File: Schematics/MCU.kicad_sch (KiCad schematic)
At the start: 24 parts, among them U1 STM32F405RGTx

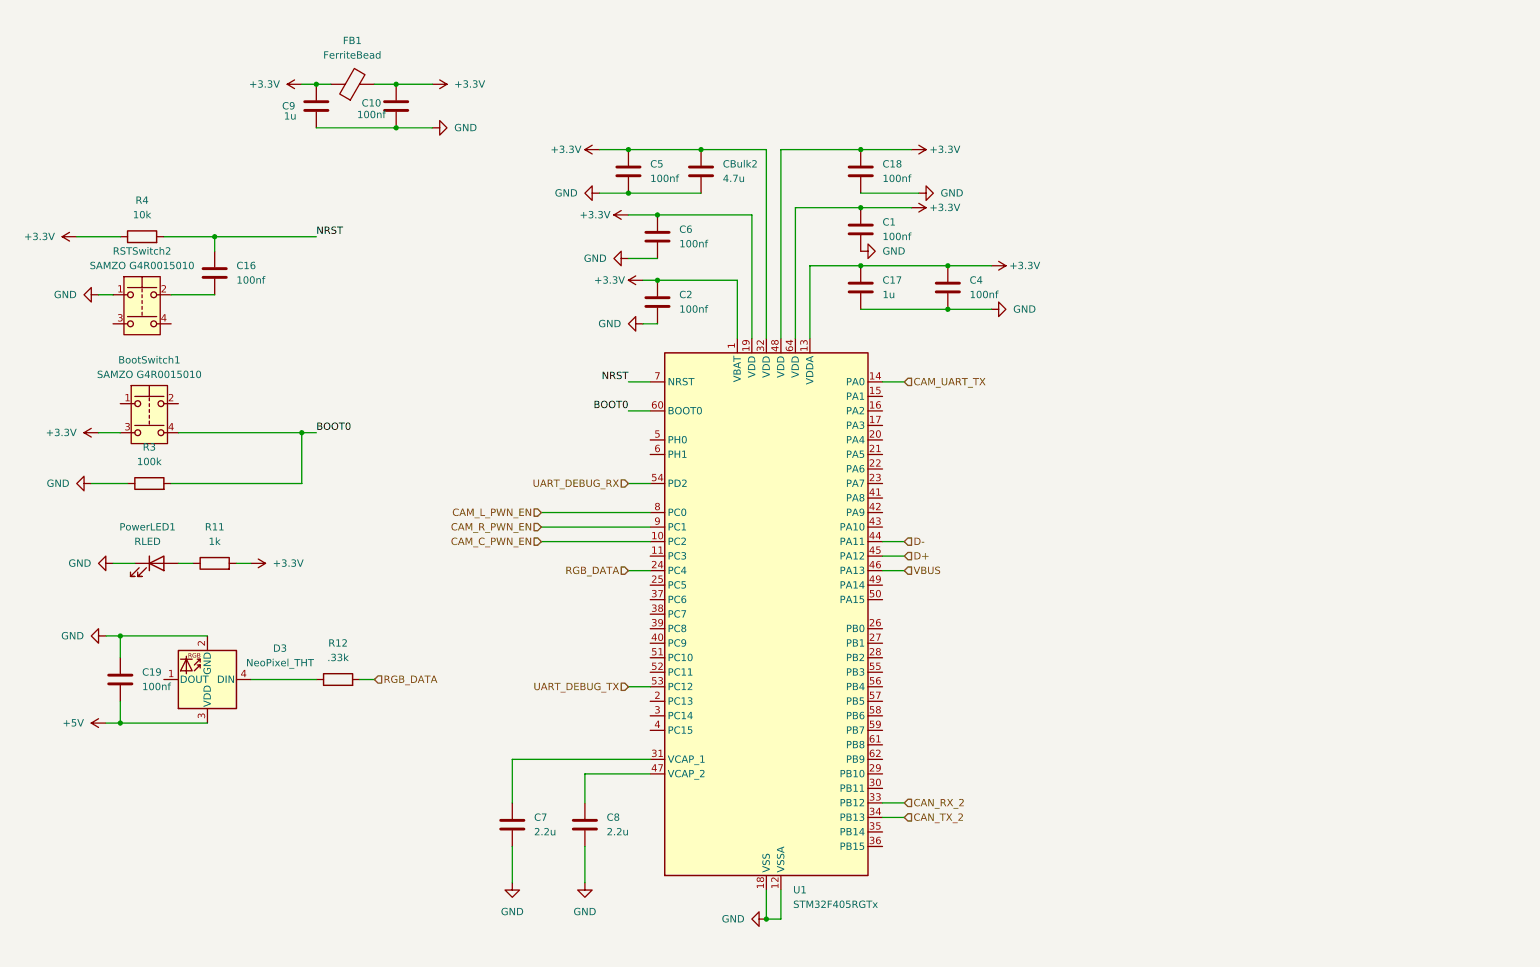
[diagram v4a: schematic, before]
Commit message: routing taking place only USB to do
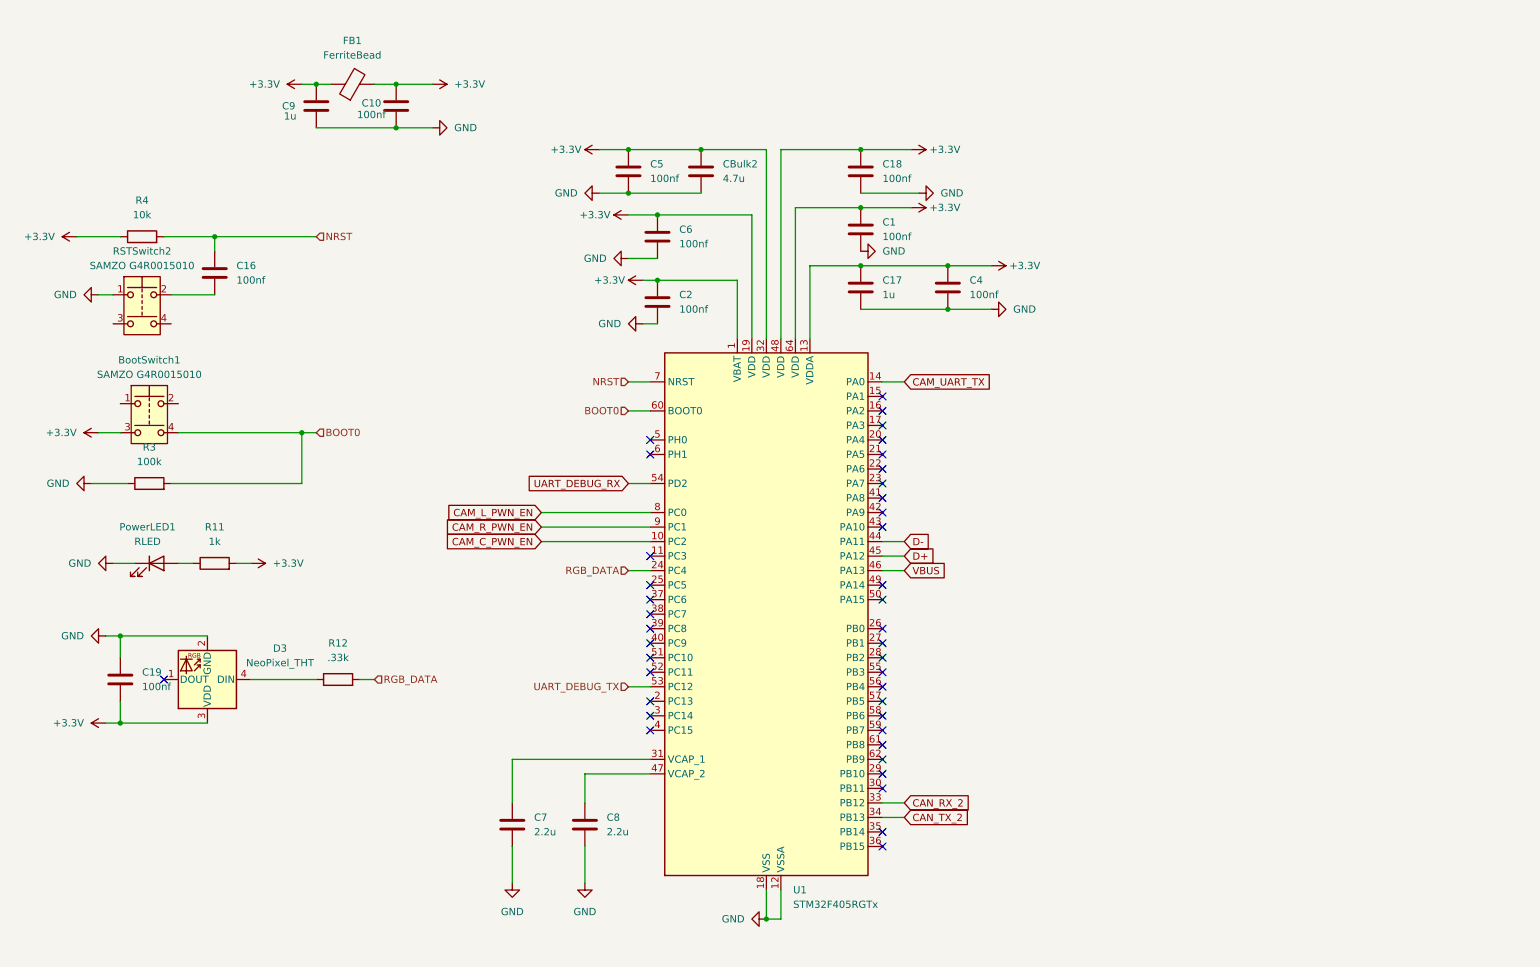
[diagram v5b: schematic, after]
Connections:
- net +5V is gone; now on net +3.3V: C19.2, D3.3 (VDD)
- no-connect marks 0 -> 40

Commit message: Cleaned up schematic added ocilator added jtag 10 pin begining routing again
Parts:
- added C21, C22: 18p, Capacitor_SMD:C_0603_1608Metric_Pad1.08x0.95mm_HandSolder, symbol Device:C
- added J1: Microsemi_FlashPro-JTAG-10, myFootprints:CONN_7024610XX_MOL, symbol Connector:Microsemi_FlashPro-JTAG-10
- added Y1: 8mhz, Crystal:Crystal_SMD_3225-4Pin_3.2x2.5mm_HandSoldering, symbol Device:Crystal_GND24
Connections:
- net +3.3V: no longer C10.2, C17.1, C4.1, FB1.2, U1.13 (VDDA)
- net GND: now also C21.2, C22.2, Y1.2, Y1.4
- net OSC IN: now reaches U1.5 (PH0)
- net OSC IN: now also C21.1, Y1.1
- net OSC OUT: now reaches U1.6 (PH1)
- net OSC OUT: now also C22.1, Y1.3
- new net: J1.10 (GND), J1.2 (GND)
- new net +3.3VA: C10.2, C17.1, C4.1, FB1.2, U1.13 (VDDA)
- no-connect marks 40 -> 38
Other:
- moved on the sheet: BootSwitch1, C19, D3, PowerLED1, R11, R12, R3

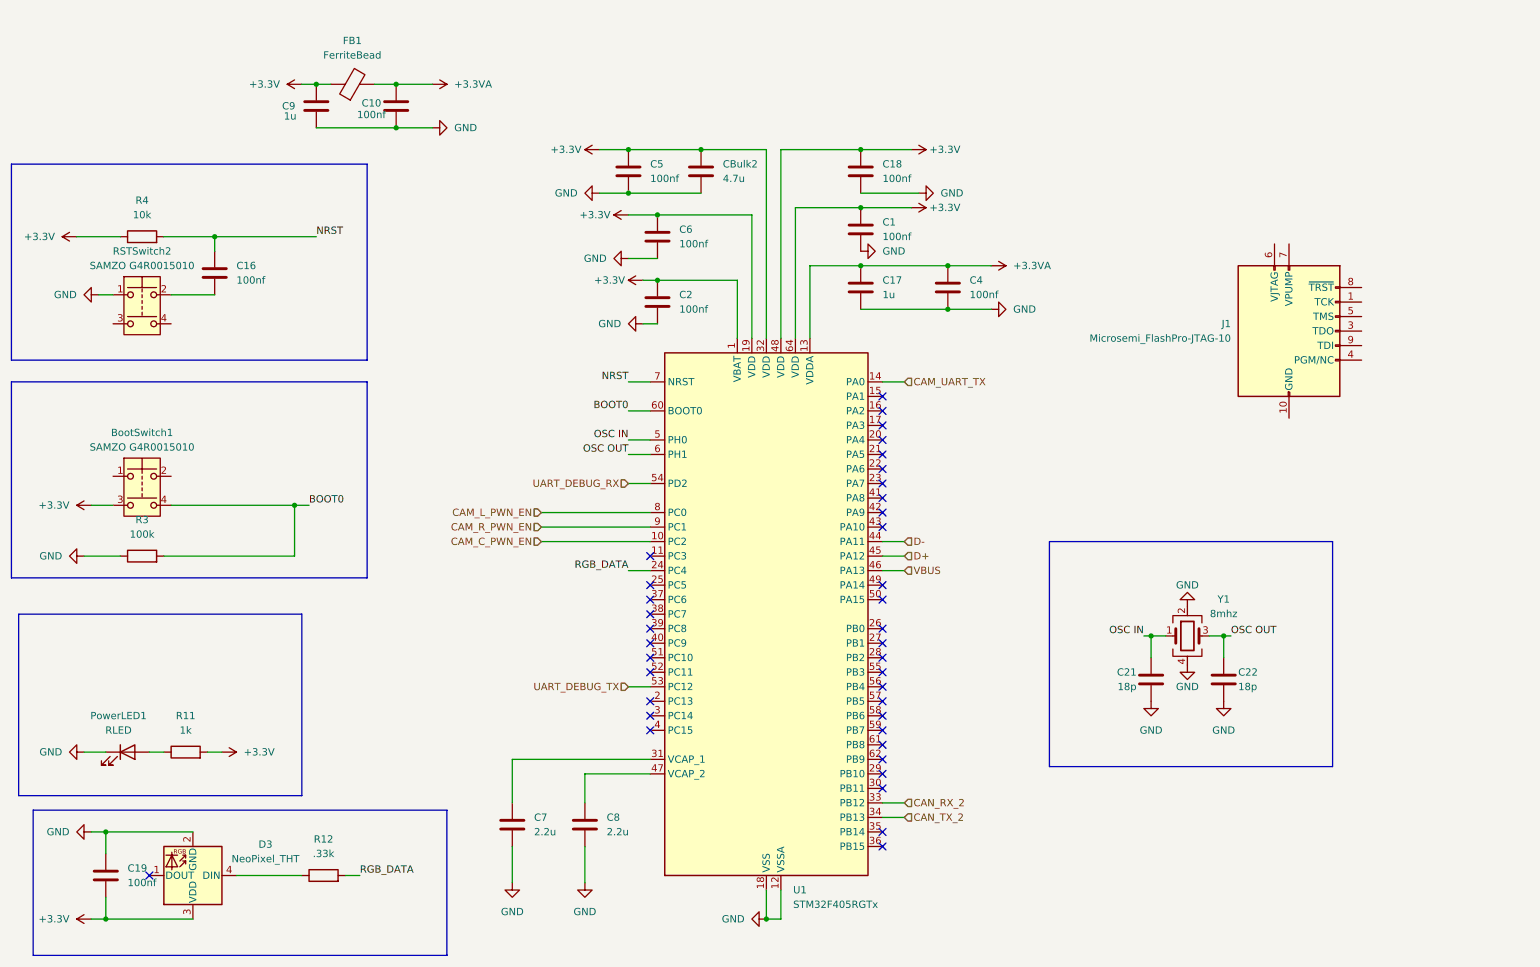
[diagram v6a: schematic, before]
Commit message: second final draft finished routing added swd debug with stlink capabilities pending review for and data sheet review to ensure parts are correct, also need to edge cut ocillator
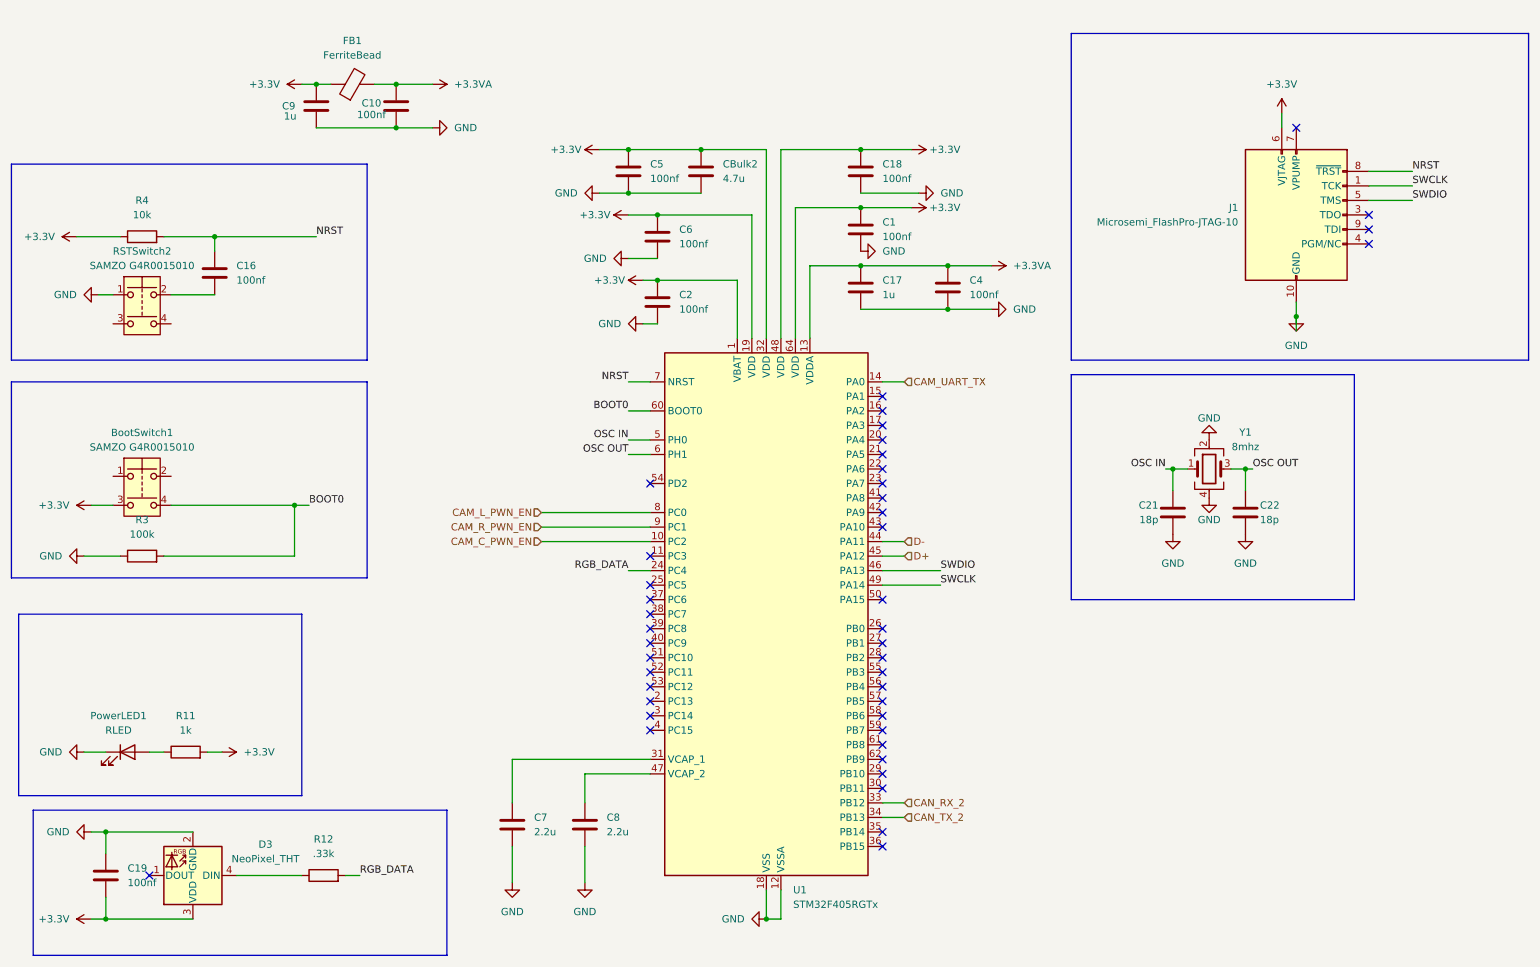
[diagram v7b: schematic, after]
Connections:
- net VBUS is gone; now on net SWDIO: U1.46 (PA13)
- net +3.3V: now also J1.6 (VJTAG)
- net GND: now also J1.10 (GND), J1.2 (GND)
- net NRST: now also J1.8 (~{TRST})
- net SWCLK: now reaches J1.1 (TCK)
- net SWCLK: now also U1.49 (PA14)
- net SWDIO: now reaches J1.5 (TMS)
- net UART_DEBUG_RX: no longer names the net of U1.54 (PD2)
- net UART_DEBUG_TX: no longer names the net of U1.53 (PC12)
- no-connect marks 38 -> 43
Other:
- moved on the sheet: C21, C22, J1, Y1

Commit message: added LCSC numbers and generated BOM, fixed schematic
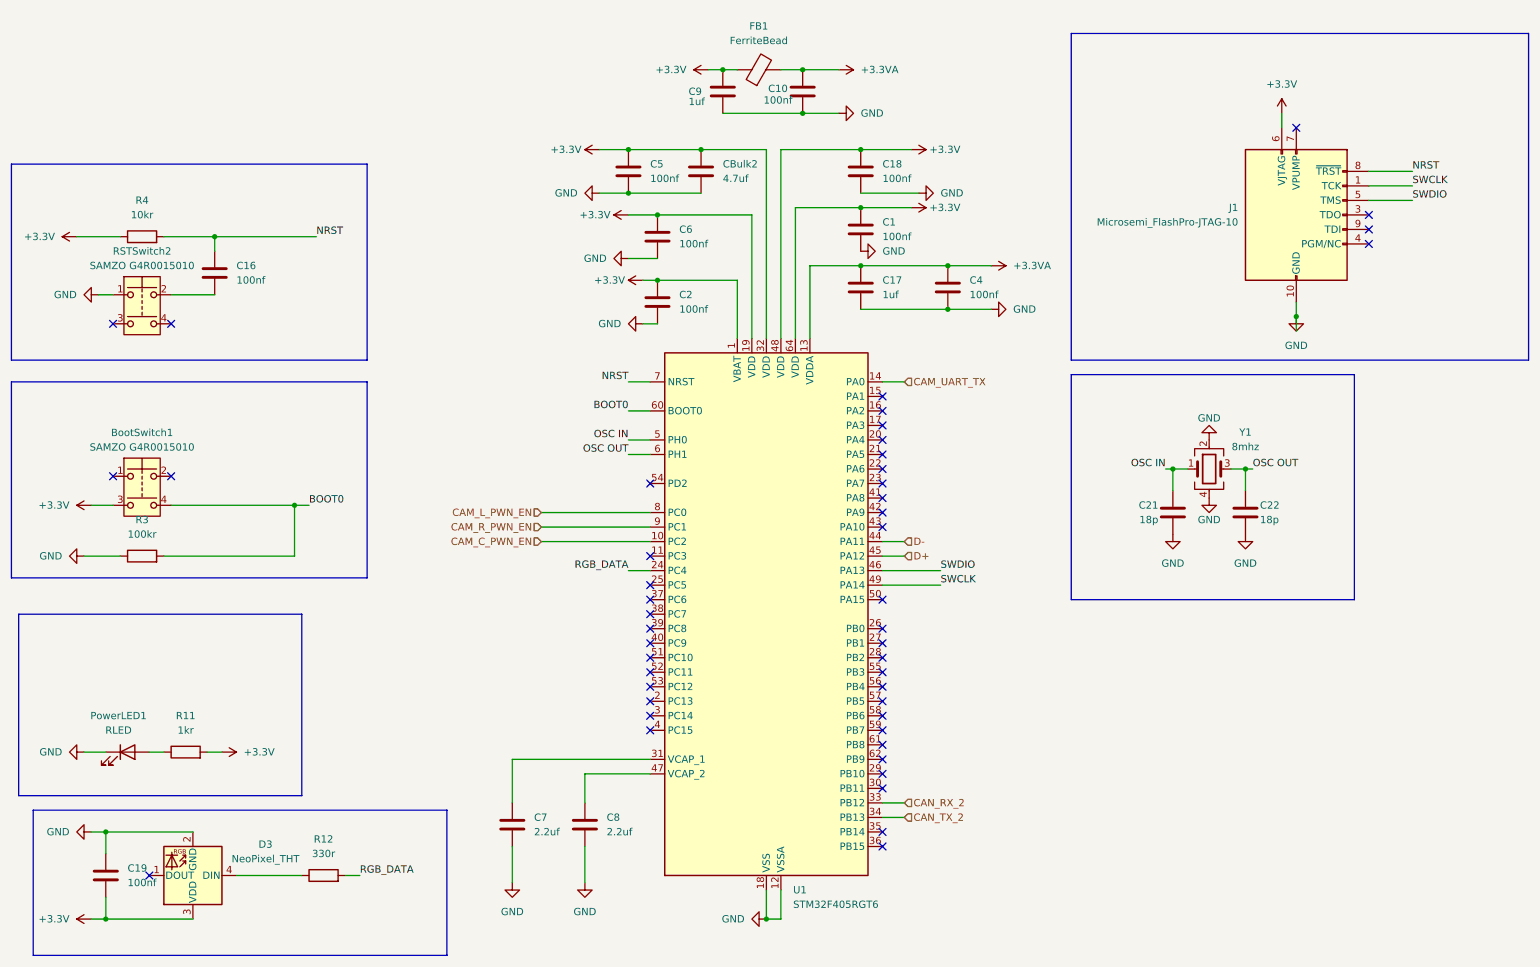
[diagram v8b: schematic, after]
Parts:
- BootSwitch1, RSTSwitch2: LCSC (none) -> C49393646
- C1, C10, C16, C18, C2, C4, C5, C6: LCSC (none) -> C49678
- C17, C9: value 1u -> 1uf; LCSC (none) -> C28323
- C19: footprint Resistor_SMD:R_0805_2012Metric_Pad1.20x1.40mm_HandSolder -> Capacitor_SMD:C_0805_2012Metric_Pad1.18x1.45mm_HandSolder; LCSC (none) -> C49393646
- C21, C22: LCSC (none) -> C53084486
- C7, C8: value 2.2u -> 2.2uf; LCSC (none) -> C19110
- CBulk2: value 4.7u -> 4.7uf; LCSC (none) -> C98192
- D3: LCSC (none) -> C2827321
- FB1: LCSC (none) -> C85840
- J1: LCSC (none) -> C588426
- PowerLED1: LCSC (none) -> C965799
- R11: value 1k -> 1kr; LCSC (none) -> C95781
- R12: value .33k -> 330r; LCSC (none) -> C17630
- R3: value 100k -> 100kr; LCSC (none) -> C96346
- R4: value 10k -> 10kr; LCSC (none) -> C84376
- U1: value STM32F405RGTx -> STM32F405RGT6; LCSC (none) -> C15742
- Y1: LCSC (none) -> C49158084
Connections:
- no-connect marks 43 -> 47
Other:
- moved on the sheet: C10, C9, FB1
